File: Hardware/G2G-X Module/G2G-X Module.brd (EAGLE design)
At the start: 13.1 x 12.8 mm, 4 parts, among them J1 GROVE-4P-2.0-3470130P1

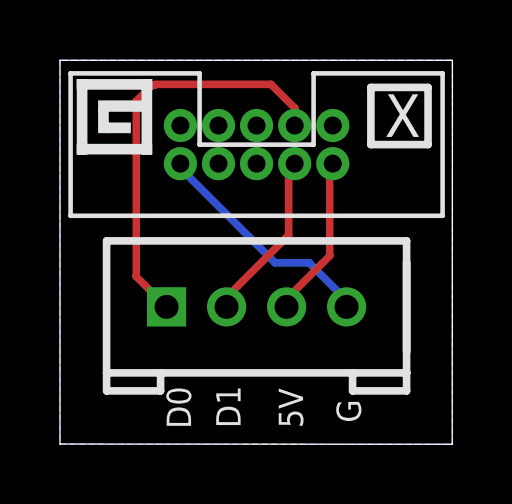
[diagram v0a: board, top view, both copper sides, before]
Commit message: Rotated the G plug 180 degrees.
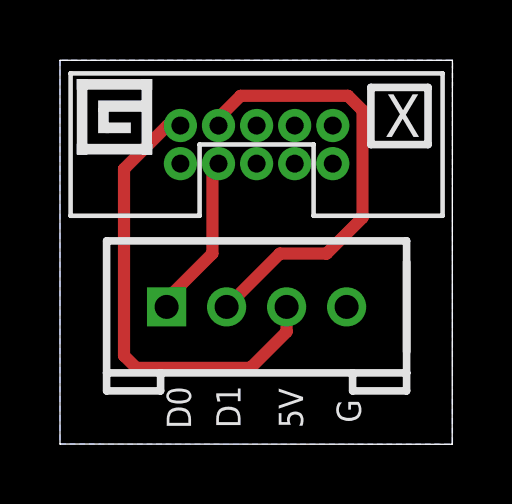
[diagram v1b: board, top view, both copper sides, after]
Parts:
- turned U$1 to 180 degrees
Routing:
- net +5V: track 5.39 -> 15.6 mm
- net D1: track 5.85 -> 14.9 mm
- net D0: track 13.7 -> 5.49 mm
- net GND: track 7.74 -> 0.00 mm
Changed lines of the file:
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@@
 <element name="J1" library="SoftDust" package="4P-2.0" value="GROVE-4P-2.0-3470130P1" x="6.5532" y="4.572" smashed="yes"/>
 <element name="LOGO1" library="SparkFun-Aesthetics" package="OSHW-LOGO-S" value="OSHW-LOGOS" x="1.8796" y="1.778" rot="MR0"/>
-<element name="U$1" library="SoftDust" package="2X5_1.27MM_FEMALE_PLUG" value="2X5_1.27MM_FEMALE_PLUG" x="6.5532" y="9.9822" rot="MR0"/>
+<element name="U$1" library="SoftDust" package="2X5_1.27MM_FEMALE_PLUG" value="2X5_1.27MM_FEMALE_PLUG" x="6.5532" y="9.9822" rot="MR180"/>
 <element name="FRAME1" library="SparkFun-Aesthetics" package="DUMMY" value="" x="0" y="-1.27">
 <attribute name="VERSION" value="v1.0" x="0" y="-1.27" size="1.778" layer="27" display="off"/>
@@
 <contactref element="U$1" pad="10"/>
 <contactref element="J1" pad="4"/>
-<wire x1="4.191" y1="9.017" x2="4.191" y2="9.2456" width="0.254" layer="16"/>
-<wire x1="7.1628" y1="6.0452" x2="4.191" y2="9.017" width="0.254" layer="16"/>
-<wire x1="8.3058" y1="6.0452" x2="7.1628" y2="6.0452" width="0.254" layer="16"/>
-<wire x1="9.4488" y1="4.9022" x2="8.3058" y2="6.0452" width="0.254" layer="16"/>
-<wire x1="4.191" y1="9.2456" x2="4.0132" y2="9.3472" width="0.254" layer="16"/>
-<wire x1="9.4488" y1="4.9022" x2="9.5532" y2="4.572" width="0.254" layer="16"/>
 <polygon width="0.254" layer="16" isolate="0.4064">
 <vertex x="0" y="0"/>
@@
 <contactref element="J1" pad="3"/>
 <contactref element="U$1" pad="2"/>
-<wire x1="8.9916" y1="6.2738" x2="8.9916" y2="9.2456" width="0.254" layer="1"/>
-<wire x1="7.62" y1="4.9022" x2="8.9916" y2="6.2738" width="0.254" layer="1"/>
-<wire x1="8.9916" y1="9.2456" x2="9.0932" y2="9.3472" width="0.254" layer="1"/>
-<wire x1="7.62" y1="4.9022" x2="7.5532" y2="4.572" width="0.254" layer="1"/>
+<wire x1="7.5532" y1="4.572" x2="7.5532" y2="3.7432" width="0.4064" layer="1"/>
+<wire x1="7.5532" y1="3.7432" x2="6.35" y2="2.54" width="0.4064" layer="1"/>
+<wire x1="6.35" y1="2.54" x2="2.54" y2="2.54" width="0.4064" layer="1"/>
+<wire x1="2.54" y1="2.54" x2="2.1336" y2="2.9464" width="0.4064" layer="1"/>
+<wire x1="2.1336" y1="2.9464" x2="2.1336" y2="9.1694" width="0.4064" layer="1"/>
+<wire x1="2.1336" y1="9.1694" x2="3.5814" y2="10.6172" width="0.4064" layer="1"/>
+<wire x1="3.5814" y1="10.6172" x2="4.0132" y2="10.6172" width="0.4064" layer="1"/>
 </signal>
 <signal name="D1">
 <contactref element="J1" pad="2"/>
 <contactref element="U$1" pad="4"/>
-<wire x1="7.62" y1="6.9596" x2="7.62" y2="9.2456" width="0.254" layer="1"/>
-<wire x1="5.5626" y1="4.9022" x2="7.62" y2="6.9596" width="0.254" layer="1"/>
-<wire x1="7.62" y1="9.2456" x2="7.8232" y2="9.3472" width="0.254" layer="1"/>
-<wire x1="5.4864" y1="4.8006" x2="5.4864" y2="4.572" width="0.254" layer="1"/>
-<wire x1="5.4864" y1="4.572" x2="5.5532" y2="4.572" width="0.254" layer="1"/>
-<wire x1="5.4864" y1="4.8006" x2="5.5626" y2="4.9022" width="0.254" layer="1"/>
+<wire x1="5.5532" y1="4.572" x2="7.3312" y2="6.35" width="0.4064" layer="1"/>
+<wire x1="7.3312" y1="6.35" x2="8.89" y2="6.35" width="0.4064" layer="1"/>
+<wire x1="8.89" y1="6.35" x2="10.0838" y2="7.5438" width="0.4064" layer="1"/>
+<wire x1="10.0838" y1="7.5438" x2="10.0838" y2="11.1252" width="0.4064" layer="1"/>
+<wire x1="10.0838" y1="11.1252" x2="9.6012" y2="11.6078" width="0.4064" layer="1"/>
+<wire x1="9.6012" y1="11.6078" x2="6.0198" y2="11.6078" width="0.4064" layer="1"/>
+<wire x1="6.0198" y1="11.6078" x2="5.2832" y2="10.8712" width="0.4064" layer="1"/>
+<wire x1="5.2832" y1="10.8712" x2="5.2832" y2="10.6172" width="0.4064" layer="1"/>
 </signal>
 <signal name="D0">
 <contactref element="U$1" pad="3"/>
 <contactref element="J1" pad="1"/>
-<wire x1="3.5532" y1="4.572" x2="2.54" y2="5.5852" width="0.254" layer="1"/>
-<wire x1="2.54" y1="5.5852" x2="2.54" y2="11.43" width="0.254" layer="1"/>
-<wire x1="2.54" y1="11.43" x2="3.0734" y2="11.9634" width="0.254" layer="1"/>
-<wire x1="3.0734" y1="11.9634" x2="3.1496" y2="11.9634" width="0.254" layer="1"/>
-<wire x1="3.1496" y1="11.9634" x2="3.175" y2="11.9888" width="0.254" layer="1"/>
-<wire x1="3.175" y1="11.9888" x2="7.0358" y2="11.9888" width="0.254" layer="1"/>
-<wire x1="7.0358" y1="11.9888" x2="7.8232" y2="11.2014" width="0.254" layer="1"/>
-<wire x1="7.8232" y1="11.2014" x2="7.8232" y2="10.6172" width="0.254" layer="1"/>
+<wire x1="3.5532" y1="4.572" x2="3.5532" y2="4.8232" width="0.4064" layer="1"/>
+<wire x1="3.5532" y1="4.8232" x2="5.08" y2="6.35" width="0.4064" layer="1"/>
+<wire x1="5.08" y1="6.35" x2="5.08" y2="9.144" width="0.4064" layer="1"/>
+<wire x1="5.08" y1="9.144" x2="5.2832" y2="9.3472" width="0.4064" layer="1"/>
 </signal>
 </signals>

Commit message: Replaced all 'G' logos with a new part for the logo.
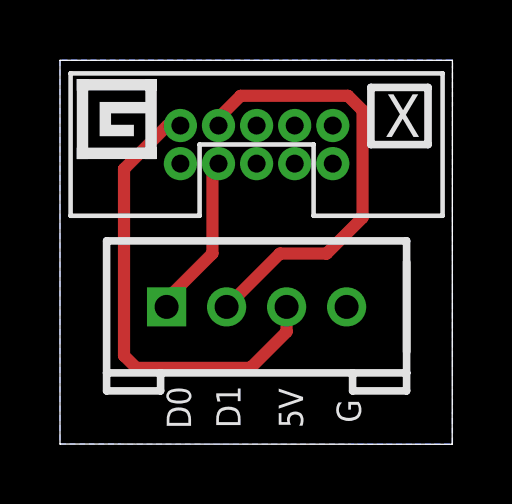
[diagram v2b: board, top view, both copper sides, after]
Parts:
- added U$2: GADGETEER_LOGO_SMALL, SoftDust:GADGETEER_LOGO_SMALL
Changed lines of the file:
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@@
 <text x="10.033" y="0.7112" size="0.8128" layer="21" font="vector" rot="R90">G</text>
 <text x="11.6586" y="5.9944" size="1.016" layer="22" font="vector" rot="MR0">Gadgeteer.in'</text>
-<rectangle x1="0.5588" y1="9.652" x2="3.0734" y2="10.0076" layer="21"/>
-<rectangle x1="0.5588" y1="11.811" x2="3.0734" y2="12.1666" layer="21"/>
-<rectangle x1="1.6383" y1="10.7315" x2="4.1529" y2="11.0871" layer="21" rot="R90"/>
-<rectangle x1="-0.5207" y1="10.7315" x2="1.9939" y2="11.0871" layer="21" rot="R90"/>
-<rectangle x1="1.27" y1="11.0744" x2="2.7432" y2="11.4554" layer="21"/>
-<rectangle x1="1.27" y1="10.3632" x2="1.6256" y2="11.2014" layer="21"/>
-<rectangle x1="1.7653" y1="10.1219" x2="2.1209" y2="10.9601" layer="21" rot="R90"/>
 </plain>
 <attributes>
@@
 <attribute name="DESIGNER" value="Ian Lee" x="0" y="-1.27" size="1.778" layer="27" display="off"/>
 </element>
+<element name="U$2" library="SoftDust" package="GADGETEER_LOGO_SMALL" value="GADGETEER_LOGO_SMALL" x="0.5588" y="9.4996"/>
 </elements>
 <signals>
